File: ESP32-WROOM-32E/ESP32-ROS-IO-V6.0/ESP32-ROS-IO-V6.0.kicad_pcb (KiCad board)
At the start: 2 copper layers, 100 x 100 mm, 56 parts, among them J1 Conn_01x19_Socket, J16 XT60-M, J17 XT60-M, J2 Conn_01x19_Socket, J3 Conn_01x19_Socket, J4 Conn_01x19_Socket, J5 Conn_01x02_Pin, J6 Conn_01x02_Pin, SW1 SW1, SW2 SW2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

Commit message: 10かけ10に収まらない
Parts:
- moved R120 64.2 mm to (126.3, 103.2)
- moved J5 64.2 mm to (117.1, 103.2)
- moved J6 64.2 mm to (121.7, 103.2)
- moved ENC2 10.1 mm to (174.6, 78.5)
- moved D1 2.72 mm to (169.9, 94.5)
- moved TBD62003APG 1.78 mm to (175.0, 104.3)
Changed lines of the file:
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@@
 	(footprint "Package_DIP:DIP-16_W7.62mm"
 		(layer "F.Cu")
-		(at 174.9806 106.0704)
+		(at 174.9806 104.2924)
 		(descr "16-lead though-hole mounted DIP package, row spacing 7.62mm (300 mils)")
 		(tags "THT DIP DIL PDIP 2.54mm 7.62mm 300mil")
@@
 	(footprint "Connector_JST:JST_XH_B4B-XH-A_1x04_P2.50mm_Vertical"
 		(layer "F.Cu")
-		(at 170.046 87.4776)
+		(at 174.6434 78.486)
 		(descr "JST XH series connector, B4B-XH-A (http://www.jst-mfg.com/product/pdf/eng/eXH.pdf), generated with kicad-footprint-generator")
 		(tags "connector JST XH vertical")
@@
 	(footprint "Connector_PinHeader_2.54mm:PinHeader_1x02_P2.54mm_Vertical"
 		(layer "F.Cu")
-		(at 179.9912 76.2)
+		(at 121.6988 103.1952)
 		(descr "Through hole straight pin header, 1x02, 2.54mm pitch, single row")
 		(tags "Through hole pin header THT 1x02 2.54mm single row")
@@
 	(footprint "Connector_PinHeader_2.54mm:PinHeader_1x02_P2.54mm_Vertical"
 		(layer "F.Cu")
-		(at 184.5812 76.2)
+		(at 126.2888 103.1952)
 		(descr "Through hole straight pin header, 1x02, 2.54mm pitch, single row")
 		(tags "Through hole pin header THT 1x02 2.54mm single row")
@@
 	(footprint "Connector_PinHeader_2.54mm:PinHeader_1x02_P2.54mm_Vertical"
 		(layer "F.Cu")
-		(at 175.4012 76.2)
+		(at 117.1088 103.1952)
 		(descr "Through hole straight pin header, 1x02, 2.54mm pitch, single row")
 		(tags "Through hole pin header THT 1x02 2.54mm single row")
@@
 	(footprint "LED_THT:LED_D5.0mm"
 		(layer "F.Cu")
-		(at 169.8752 97.2312)
+		(at 169.8752 94.5134)
 		(descr "LED, diameter 5.0mm, 2 pins, http://cdn-reichelt.de/documents/datenblatt/A500/LL-504BC2E-009.pdf, generated by kicad-footprint-generator")
 		(tags "LED")

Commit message: しるく
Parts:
- moved MCP2561 60.2 mm to (117.8, 109.2)
- moved G***6 24.0 mm to (170.6, 135.8)
- moved ENC3 7.08 mm to (120.9, 145.2), turned to 90 degrees
- moved ENC4 6.74 mm to (179.2, 138.3), turned to -90 degrees
- moved J5 2.49 mm to (117.1, 100.7)
- moved J6 2.49 mm to (121.7, 100.7)
- moved R120 2.49 mm to (126.3, 100.7)
- moved R1 1.17 mm to (119.3, 132.0)
- moved R2 1.17 mm to (123.3, 132.0)
- moved TBD62003APG 0.86 mm to (174.1, 104.3)
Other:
- board text added: "+ GND"
- board text added: "5V0 G A B"
- board text added: "H L"
- board text added: "S + GND"

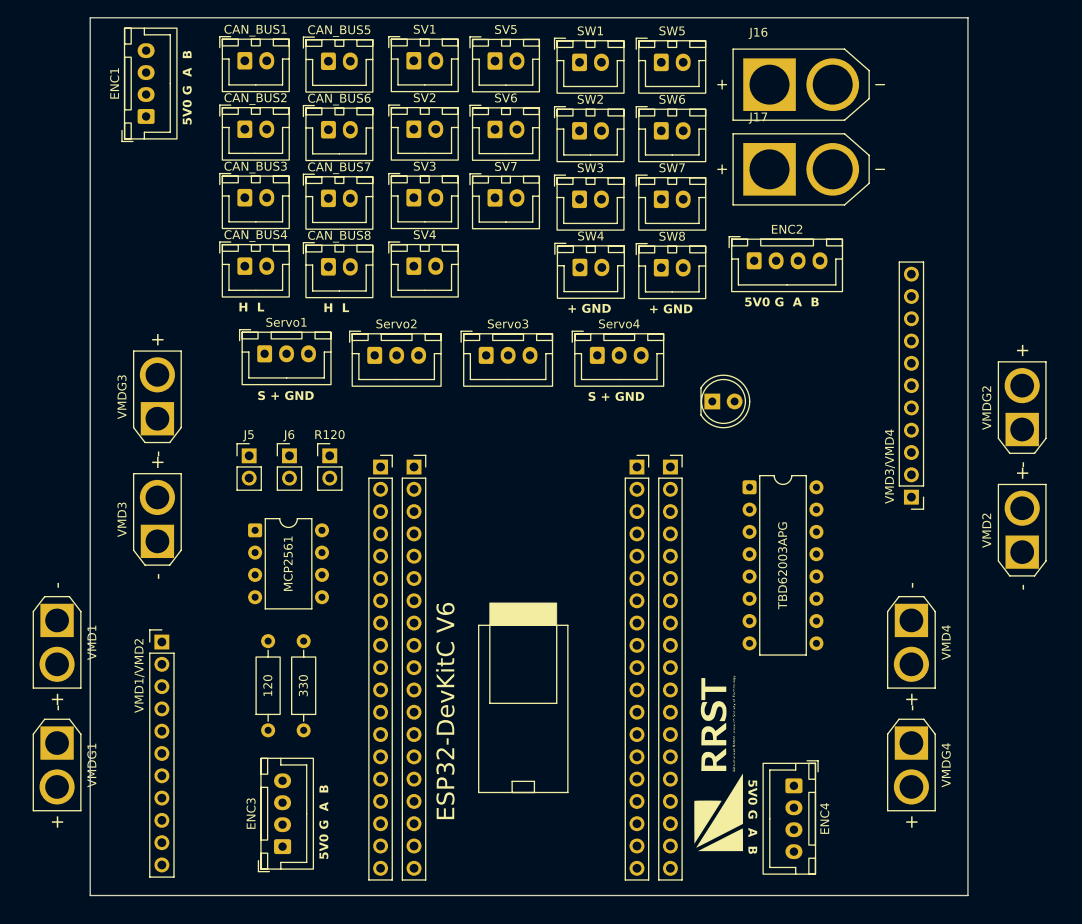
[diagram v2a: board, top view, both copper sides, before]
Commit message: 10×10に収まらないだけでそれ以外はできた
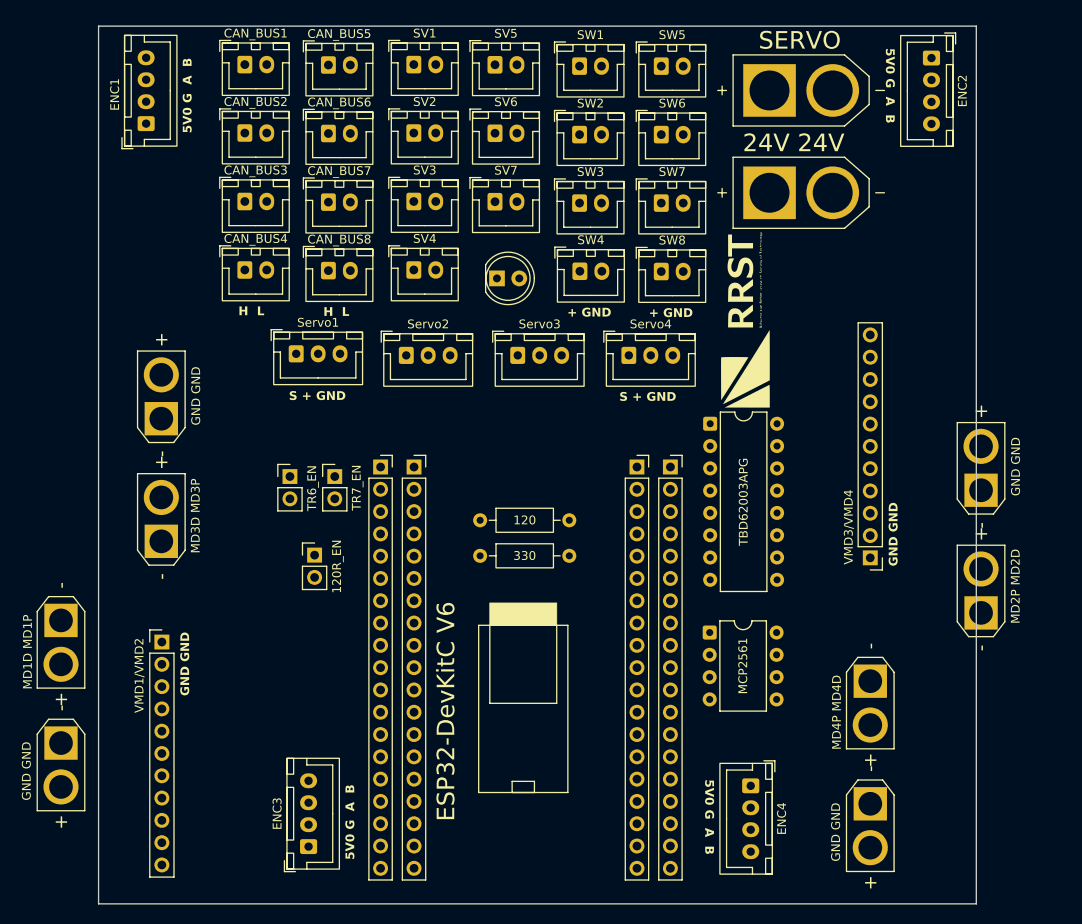
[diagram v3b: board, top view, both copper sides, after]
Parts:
- removed J5, J6: Conn_01x02_Pin, Connector_PinHeader_2.54mm:PinHeader_1x02_P2.54mm_Vertical
- added TR6_EN: Conn_01x02_Pin, Connector_PinHeader_2.54mm:PinHeader_1x02_P2.54mm_Vertical, F.Cu at (121.8, 103.1)
- added TR7_EN: Conn_01x02_Pin, Connector_PinHeader_2.54mm:PinHeader_1x02_P2.54mm_Vertical, F.Cu at (126.9, 103.1)
- moved MCP2561 53.1 mm to (169.6, 120.8)
- moved G***6 50.6 mm to (173.7, 85.2)
- moved R1 34.0 mm to (143.4, 108.0), turned to 0 degrees
- moved ENC2 30.7 mm to (194.8, 55.4), turned to -90 degrees
- moved R2 28.3 mm to (143.4, 112.1), turned to 0 degrees
- moved D1 28.3 mm to (145.3, 80.5)
- moved 120R_EN 11.4 mm to (124.6, 112.0)
- moved TBD62003APG 8.52 mm to (169.6, 97.1)
- moved VMD3/VMD4 8.36 mm to (187.9, 112.3)
- moved VMD4 8.36 mm to (187.9, 126.4)
- moved VMDG2 8.36 mm to (200.5, 104.6)
- moved VMD2 8.36 mm to (200.5, 118.6)
- moved VMDG4 8.36 mm to (187.9, 140.3)
- moved ENC4 4.92 mm to (174.2, 138.3)
- moved Servo1 3.60 mm to (122.5, 89.1)
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- renumbered R120 to 120R_EN
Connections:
- TBD62003APG pad 7: TR6_Bypass_OUT -> TR7
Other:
- board text added: "24V 24V"
- board text added: "GND GND"
- board text added: "MD1D MD1P"
- board text added: "MD2P MD2D"
- board text added: "MD3D MD3P"
- board text added: "MD4P MD4D"
- board text added: "SERVO"

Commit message: 考え中
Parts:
- moved 120R_EN 68.6 mm to (184.4, 78.5)
- moved G***6 58.5 mm to (125.2, 118.1)
- moved TR6_EN 57.9 mm to (174.2, 78.5)
- moved TR7_EN 57.9 mm to (179.3, 78.5)
- moved Servo4 40.2 mm to (195.6, 69.8), turned to -90 degrees
- moved Servo1 22.8 mm to (104.6, 74.9), turned to 90 degrees
- moved VMD3/VMD4 18.5 mm to (206.3, 112.3)
- moved VMD3 18.0 mm to (116.8, 125.6)
- moved VMDG3 18.0 mm to (116.8, 111.7)
- moved VMD1/VMD2 12.4 mm to (94.7, 121.9)
- moved VMD1 11.8 mm to (105.3, 126.3)
- moved VMDG1 11.8 mm to (105.3, 140.2)
- moved VMD2 8.16 mm to (194.8, 124.5)
- moved VMDG2 8.16 mm to (194.8, 110.5)
- moved VMD4 4.48 mm to (183.4, 126.4)
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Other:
- board text added: "+"
- board text added: "-"
- board text added: "B A G 5V0"
- board text added: "GND + S"

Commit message: どうにかする
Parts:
- moved Servo4 40.2 mm to (160.3, 89.3), turned to 0 degrees
- moved Servo1 22.8 mm to (122.5, 89.1), turned to 0 degrees
- moved VMD3/VMD4 18.4 mm to (189.1, 118.7)
- moved VMD1/VMD2 15.1 mm to (109.9, 121.9)
- moved VMD1 0.55 mm to (104.8, 126.2)
- moved VMDG1 0.55 mm to (104.8, 140.2)
- moved VMD2 0.25 mm to (195.1, 124.5)
- moved VMDG2 0.25 mm to (195.1, 110.5)
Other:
- board text removed: "GND + S"

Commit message: 配線前
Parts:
- moved ENC2 87.0 mm to (108.9, 63.8), turned to 90 degrees
- moved SW5 54.6 mm to (120.6, 89.4)
- moved Servo1 54.4 mm to (165.7, 56.2)
- moved SW6 41.7 mm to (130.9, 89.4)
- moved Servo2 39.7 mm to (165.7, 64.1)
- moved SW7 28.8 mm to (141.2, 89.4)
- moved Servo3 25.0 mm to (165.7, 71.9)
- moved SW8 16.1 mm to (151.1, 89.3)
- moved Servo4 11.0 mm to (165.7, 79.7)
- moved ENC1 5.32 mm to (99.3, 63.8)
- moved J16 5.13 mm to (185.1, 59.1)
- moved J17 5.13 mm to (185.1, 70.7)
- moved 120R_EN 5.13 mm to (189.5, 78.5)
- moved TR6_EN 5.13 mm to (179.3, 78.5)
- moved TR7_EN 5.13 mm to (184.5, 78.5)
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
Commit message: 配線後
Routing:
- net SERVO+: track 0.00 -> 75.6 mm
- net GND: track 0.00 -> 62.0 mm
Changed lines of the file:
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@@
 		)
+	)
+	(segment
+		(start 175.4632 65.3542)
+		(end 175.4632 71.9074)
+		(width 4)
+		(layer "F.Cu")
+		(net 6)
+	)
+	(segment
+		(start 175.4632 79.6544)
+		(end 170.6772 79.6544)
+		(width 2)
+		(layer "F.Cu")
+		(net 6)
+	)
+	(segment
+		(start 175.4632 56.2356)
+		(end 170.728 56.2356)
+		(width 2)
+		(layer "F.Cu")
+		(net 6)
+	)
+	(segment
+		(start 170.688 71.9158)
+		(end 175.4548 71.9158)
+		(width 2)
+		(layer "F.Cu")
+		(net 6)
+	)
+	(segment
+		(start 175.4548 71.9158)
+		(end 175.4632 71.9074)
+		(width 0.2)
+		(layer "F.Cu")
+		(net 6)
+	)
+	(segment
+		(start 188.722 65.3542)
+		(end 175.4632 65.3542)
+		(width 4)
+		(layer "F.Cu")
+		(net 6)
+	)
+	(segment
+		(start 188.722 59.0804)
+		(end 188.722 65.3542)
+		(width 4)
+		(layer "F.Cu")
+		(net 6)
+	)
+	(segment
+		(start 175.4632 71.9074)
+		(end 175.4632 79.6544)
+		(width 4)
+		(layer "F.Cu")
+		(net 6)
+	)
+	(segment
+		(start 175.4632 64.1096)
+		(end 175.4632 56.2356)
+		(width 4)
+		(layer "F.Cu")
+		(net 6)
+	)
+	(segment
+		(start 170.688 64.0926)
+		(end 175.4462 64.0926)
+		(width 2)
+		(layer "F.Cu")
+		(net 6)
+	)
+	(segment
+		(start 175.4632 65.3542)
+		(end 175.4632 64.1096)
+		(width 4)
+		(layer "F.Cu")
+		(net 6)
+	)
+	(segment
+		(start 175.4462 64.0926)
+		(end 175.4632 64.1096)
+		(width 0.2)
+		(layer "F.Cu")
+		(net 6)
+	)
+	(segment
+		(start 168.228 56.2356)
+		(end 168.228 58.9788)
+		(width 2)
+		(layer "B.Cu")
+		(net 42)
+	)
+	(segment
+		(start 181.522 65.2272)
+		(end 181.4966 65.2526)
+		(width 0.2)
+		(layer "B.Cu")
+		(net 42)
+	)
+	(segment
+		(start 168.188 74.6506)
+		(end 175.4632 74.6506)
+		(width 2)
+		(layer "B.Cu")
+		(net 42)
+	)
+	(segment
+		(start 175.4632 82.3722)
+		(end 175.4632 74.6506)
+		(width 4)
+		(layer "B.Cu")
+		(net 42)
+	)
+	(segment
+		(start 175.4378 58.9788)
+		(end 175.4632 59.0042)
+		(width 0.2)
+		(layer "B.Cu")
+		(net 42)
+	)
+	(segment
+		(start 175.4632 65.2526)
+		(end 175.4632 59.0042)
+		(width 4)
+		(layer "B.Cu")
+		(net 42)
+	)
+	(segment
+		(start 181.4966 65.2526)
+		(end 175.4632 65.2526)
+		(width 4)
+		(layer "B.Cu")
+		(net 42)
+	)
+	(segment
+		(start 168.188 66.8528)
+		(end 175.4632 66.8528)
+		(width 2)
+		(layer "B.Cu")
+		(net 42)
+	)
+	(segment
+		(start 175.4632 66.8528)
+		(end 175.4632 74.6506)
+		(width 4)
+		(layer "B.Cu")
+		(net 42)
+	)
+	(segment
+		(start 168.1772 82.3684)
+		(end 175.4594 82.3684)
+		(width 2)
+		(layer "B.Cu")
+		(net 42)
+	)
+	(segment
+		(start 181.522 59.0804)
+		(end 181.522 65.2272)
+		(width 4)
+		(layer "B.Cu")
+		(net 42)
+	)
+	(segment
+		(start 168.188 71.9158)
+		(end 168.188 74.6506)
+		(width 2)
+		(layer "B.Cu")
+		(net 42)
+	)
+	(segment
+		(start 168.228 58.9788)
+		(end 175.4378 58.9788)
+		(width 2)
+		(layer "B.Cu")
+		(net 42)
+	)
+	(segment
+		(start 168.188 64.0926)
+		(end 168.188 66.8528)
+		(width 2)
+		(layer "B.Cu")
+		(net 42)
+	)
+	(segment
+		(start 175.4632 65.2526)
+		(end 175.4632 66.8528)
+		(width 4)
+		(layer "B.Cu")
+		(net 42)
+	)
+	(segment
+		(start 175.4594 82.3684)
+		(end 175.4632 82.3722)
+		(width 0.2)
+		(layer "B.Cu")
+		(net 42)
+	)
+	(segment
+		(start 168.1772 79.6544)
+		(end 168.1772 82.3684)
+		(width 2)
+		(layer "B.Cu")
+		(net 42)
 	)
 	(group ""

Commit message: 自動配線前
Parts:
- added REF**1: MountingHole_3.2mm_M3, MountingHole:MountingHole_3.2mm_M3, F.Cu at (121.0, 100.0)
- added REF**2: MountingHole_3.2mm_M3, MountingHole:MountingHole_3.2mm_M3, F.Cu at (167.0, 90.0)
- added REF**3: MountingHole_3.2mm_M3, MountingHole:MountingHole_3.2mm_M3, F.Cu at (167.0, 132.0)
- added REF**4: MountingHole_3.2mm_M3, MountingHole:MountingHole_3.2mm_M3, F.Cu at (121.0, 130.0)
- moved G***6 3.11 mm to (122.0, 115.0)
- moved MCP2561 2.38 mm to (163.8, 118.5)
- moved ENC3 1.72 mm to (120.1, 146.9)
- moved ENC4 1.20 mm to (167.9, 139.5)
- moved TBD62003APG 0.83 mm to (163.8, 96.2)
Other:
- outline, holes or cut-outs redrawn
